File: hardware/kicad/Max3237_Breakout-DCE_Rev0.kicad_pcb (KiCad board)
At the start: 2 copper layers, 31.8 x 51.4 mm, 13 parts, among them J1 TTL_HEADER, J2 DE9_RS232, J3 MBAUD, J4 ENABLE, J5 SHUTDOWN, U1 MAX3237EIPWR

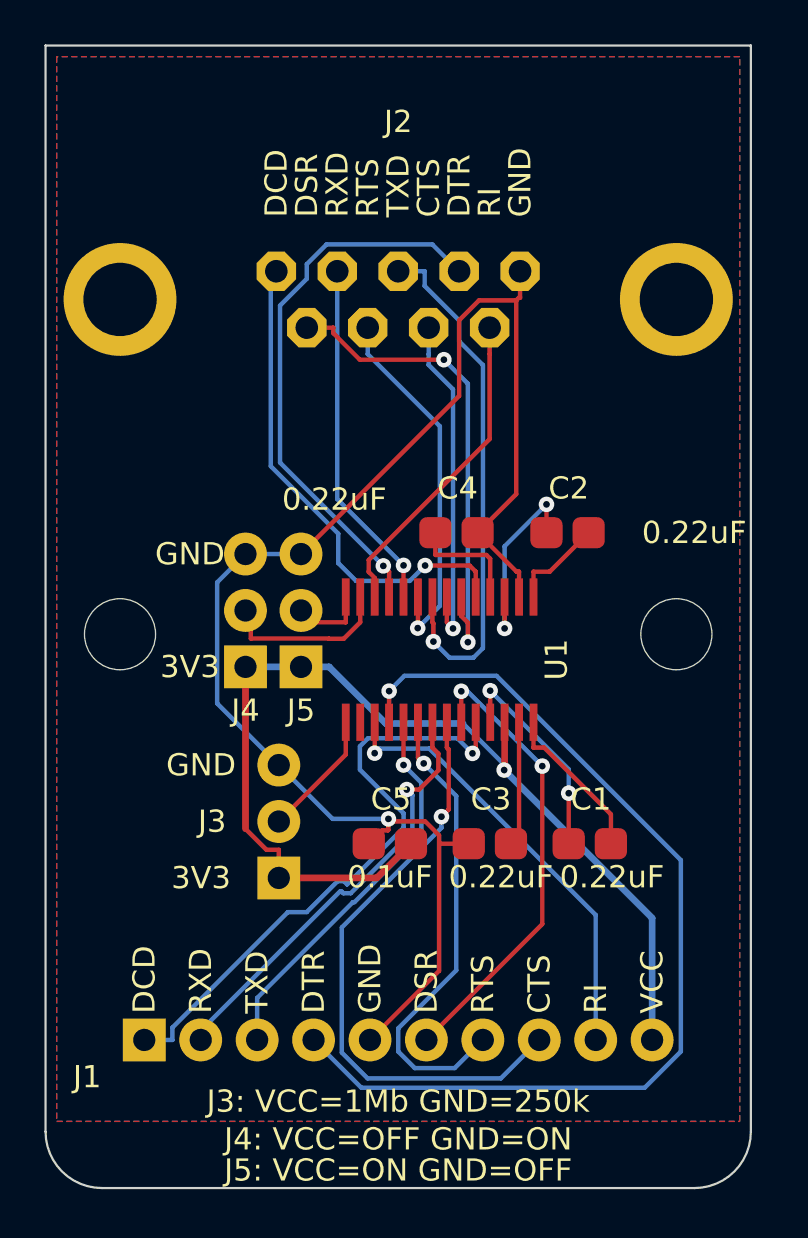
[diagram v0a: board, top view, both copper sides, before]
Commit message: Fix mirrored DE-9 (J2) footprint pinout, full copper rip/reroute/repour
The custom MAX3237_DCE:DE9_Female_THT footprint had pins 1-5 and 6-9
running in mirror-image order versus a real DE-9 connector - confirmed
by direct pad-coordinate comparison against KiCad's own standard
Connector_Dsub library part (the one the schematic's own Footprint
field already claimed to use). Left uncorrected, a real connector
soldered to this footprint would deliver: this board's DCD driver
shorted onto the cable's real signal ground (pin 1<->5 swap), RXD
fighting the peer's DTR driver, and CTS fighting the peer's RTS driver
(pin 2<->4 and 7<->8 swaps) - genuine driver-vs-driver and
driver-vs-ground contention with real RS-232 voltages present.

Fix: negate each of the 9 signal pads' local X coordinate (net
assignments unchanged) - verified against the standard library
footprint's own pin ordering before applying.

Moving the pads detached all existing copper from them, so the whole
board was ripped up and re-routed fresh via Freerouting (single
threaded, 100 max passes, Global update strategy) rather than patching
individual traces, since the footprint's physical envelope changed and
a partial patch risked missing something. Both GND pour zones
(F.Cu/B.Cu) refilled afterward. 4 auto-router fanout stubs came back
undersized (0.15mm vs the board's 0.2mm minimum, a known Freerouting
quirk) and were widened. Final DRC: 0 unconnected items, 0 electrical
violations (13 pre-existing lib_footprint_mismatch/lib_footprint_issues
warnings remain - environment footprint-library path config, unrelated
to this fix and present before it).

Co-Authored-By: Claude Sonnet 5 <noreply@anthropic.com>
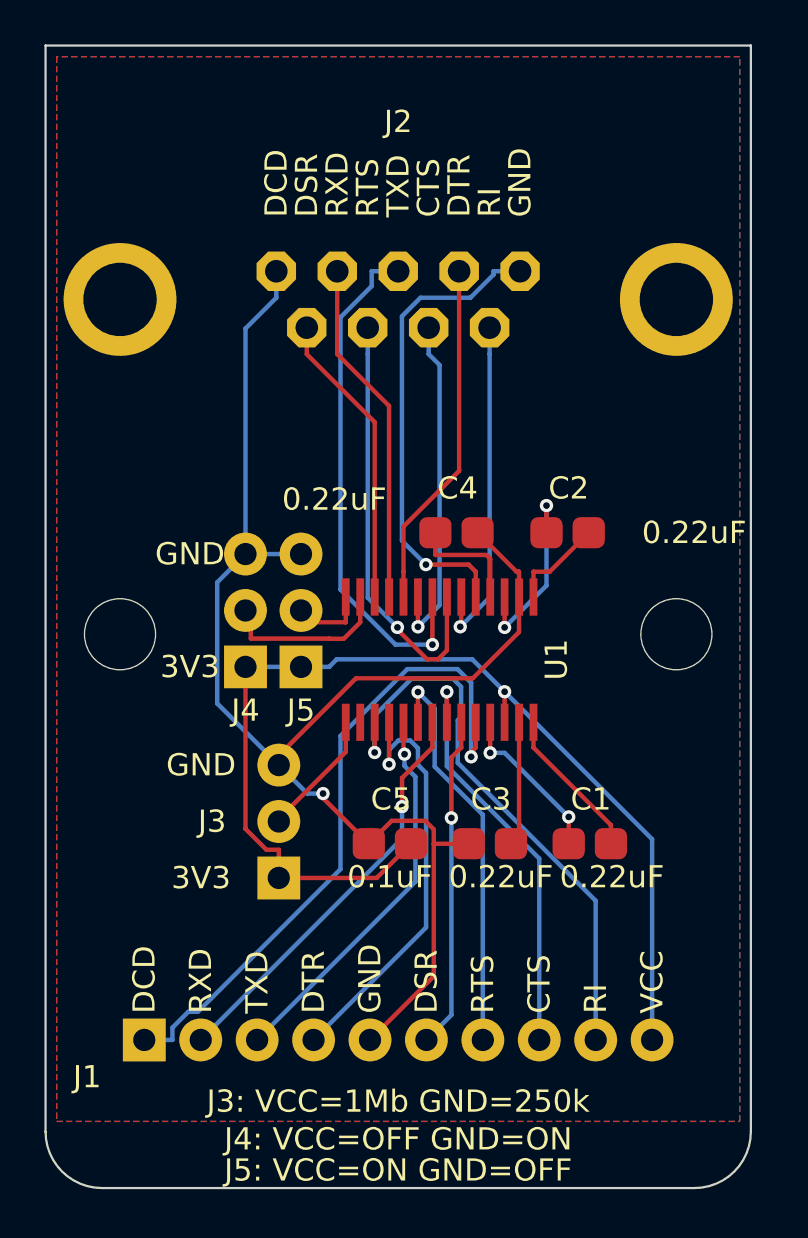
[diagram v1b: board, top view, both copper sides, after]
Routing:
- net /TTL-DTR: track 45.0 -> 19.5 mm
- net /RS232-DTR: track 25.2 -> 15.6 mm, vias 1 -> 0
- net /TTL-CTS: track 27.0 -> 18.8 mm
- net /RS232-DSR: track 22.2 -> 15.4 mm, vias 2 -> 1
- net /TTL-RI: track 20.2 -> 26.3 mm
- net /TTL-DSR: track 20.9 -> 15.0 mm, vias 2 -> 1
- net /RS232-CTS: track 15.5 -> 19.5 mm
- net /TTL-DCD: track 27.5 -> 30.7 mm
- net /TTL-RTS: track 21.3 -> 18.2 mm
- net /MAX-C1-: track 9.77 -> 7.31 mm
- net +3.3V: track 47.8 -> 49.2 mm
- net /RS232-RTS: track 16.7 -> 15.4 mm
- net /RS232-DCD: track 22.6 -> 21.4 mm
- net /TTL-RXD: track 19.8 -> 18.6 mm
- net GND: track 68.4 -> 67.2 mm
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
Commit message: Complete J2 footprint fix: correct row-to-edge orientation
The previous fix (0a0792f) only corrected J2's left-right pin order.
That check compared left-right pad rank against KiCad's standard
Connector_Dsub footprint but never verified which physical row (5-pin
vs 4-pin) sits nearer the board edge - so boards built from that
revision alone still had the 5-pin row nearer the edge instead of the
4-pin row, the same defect as the original manufactured board.

Rotate J2 the remaining 180 degrees (full 2-D pad geometry now
verified against the standard footprint, not just left-right rank,
and cross-checked against the net-name silkscreen labels), reposition
its silkscreen accordingly, and rip/reroute/repour all copper again.

Also assign standard KiCad 3D models to every footprint (previously
none had any) and regenerate docs/board_front.png and
docs/board_back.png as populated renders instead of bare-board ones.

Co-Authored-By: Claude Sonnet 5 <noreply@anthropic.com>
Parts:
- turned J2 to 180 degrees
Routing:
- net /RS232-DSR: track 15.4 -> 31.0 mm
- net /TTL-TXD: track 17.5 -> 29.4 mm, vias 1 -> 0
- net /RS232-CTS: track 19.5 -> 31.0 mm, vias 1 -> 0
- net /RS232-RTS: track 15.4 -> 24.7 mm
- net GND: track 67.2 -> 58.7 mm
- net /TTL-DCD: track 30.7 -> 22.7 mm
- net /RS232-RI: track 13.4 -> 19.7 mm, vias 0 -> 2
- net /RS232-DCD: track 21.4 -> 17.0 mm
- net /TTL-DTR: track 19.5 -> 15.7 mm, vias 1 -> 2
- net /RS232-RXD: track 15.7 -> 13.4 mm, vias 0 -> 1
- net /TTL-RXD: track 18.6 -> 20.5 mm
- net /RS232-TXD: track 23.4 -> 22.1 mm
- net /RS232-DTR: track 15.6 -> 16.9 mm, vias 0 -> 1
- net /MAX-EN: track 7.74 -> 7.03 mm
- net /TTL-DSR: track 15.0 -> 15.6 mm
